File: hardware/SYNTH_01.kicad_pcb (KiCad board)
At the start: 2 copper layers, 112.7 x 150 mm, 100 parts, among them J2 Conn_01x04_Pin, SW1 SW_Push_45deg, SW10 SW_Push_45deg, SW11 SW_Push_45deg, SW12 SW_Push_45deg, SW13 SW_Push_45deg, SW14 SW_Push_45deg, SW15 SW_Push_45deg, SW16 SW_Push_45deg, SW17 SW_Push_45deg, SW18 SW_Push_45deg, SW19 SW_Push_45deg, SW2 SW_Push_45deg, SW20 SW_Push_45deg, SW21 SW_Push_45deg, SW3 SW_Push_45deg, SW4 SW_Push_45deg, SW5 SW_Push_45deg, SW6 SW_Push_45deg, SW7 SW_Push_45deg, SW8 SW_Push_45deg, SW9 SW_Push_45deg, U1 MCP23017-E/SP, U2 74AHCT1G125

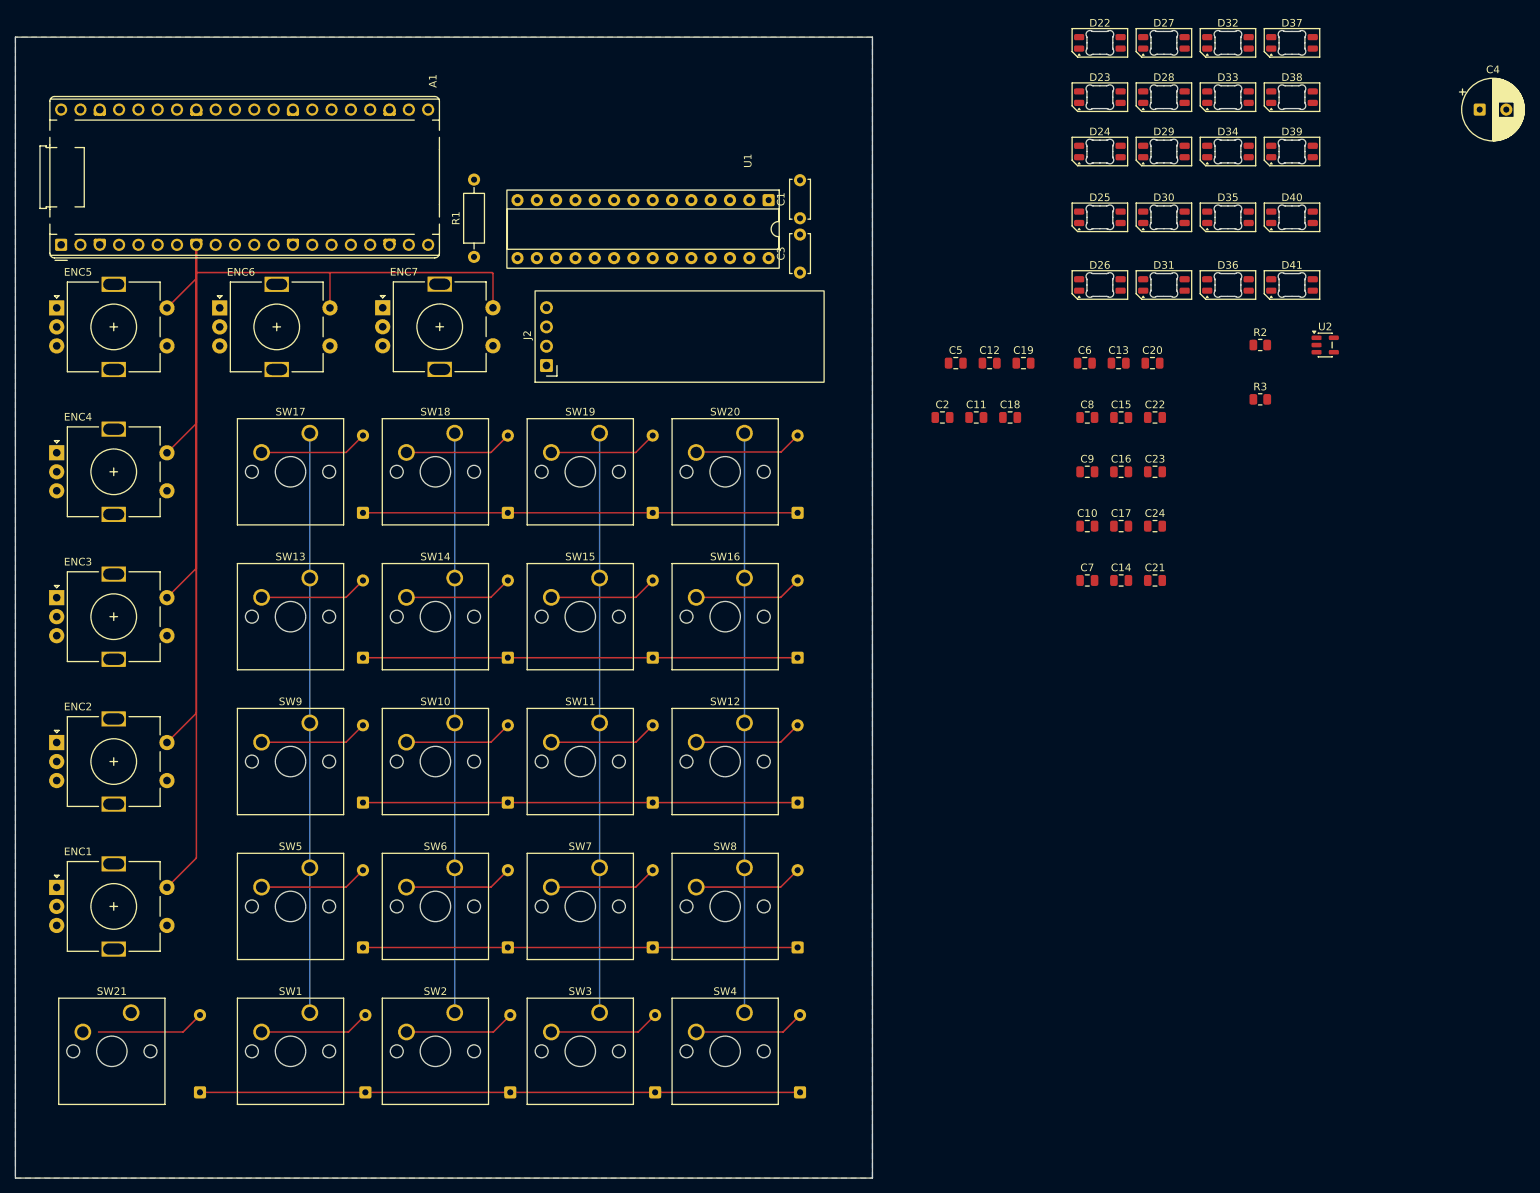
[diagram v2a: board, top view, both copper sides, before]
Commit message: PCB: connecting LEDs and their condensers in PCB view
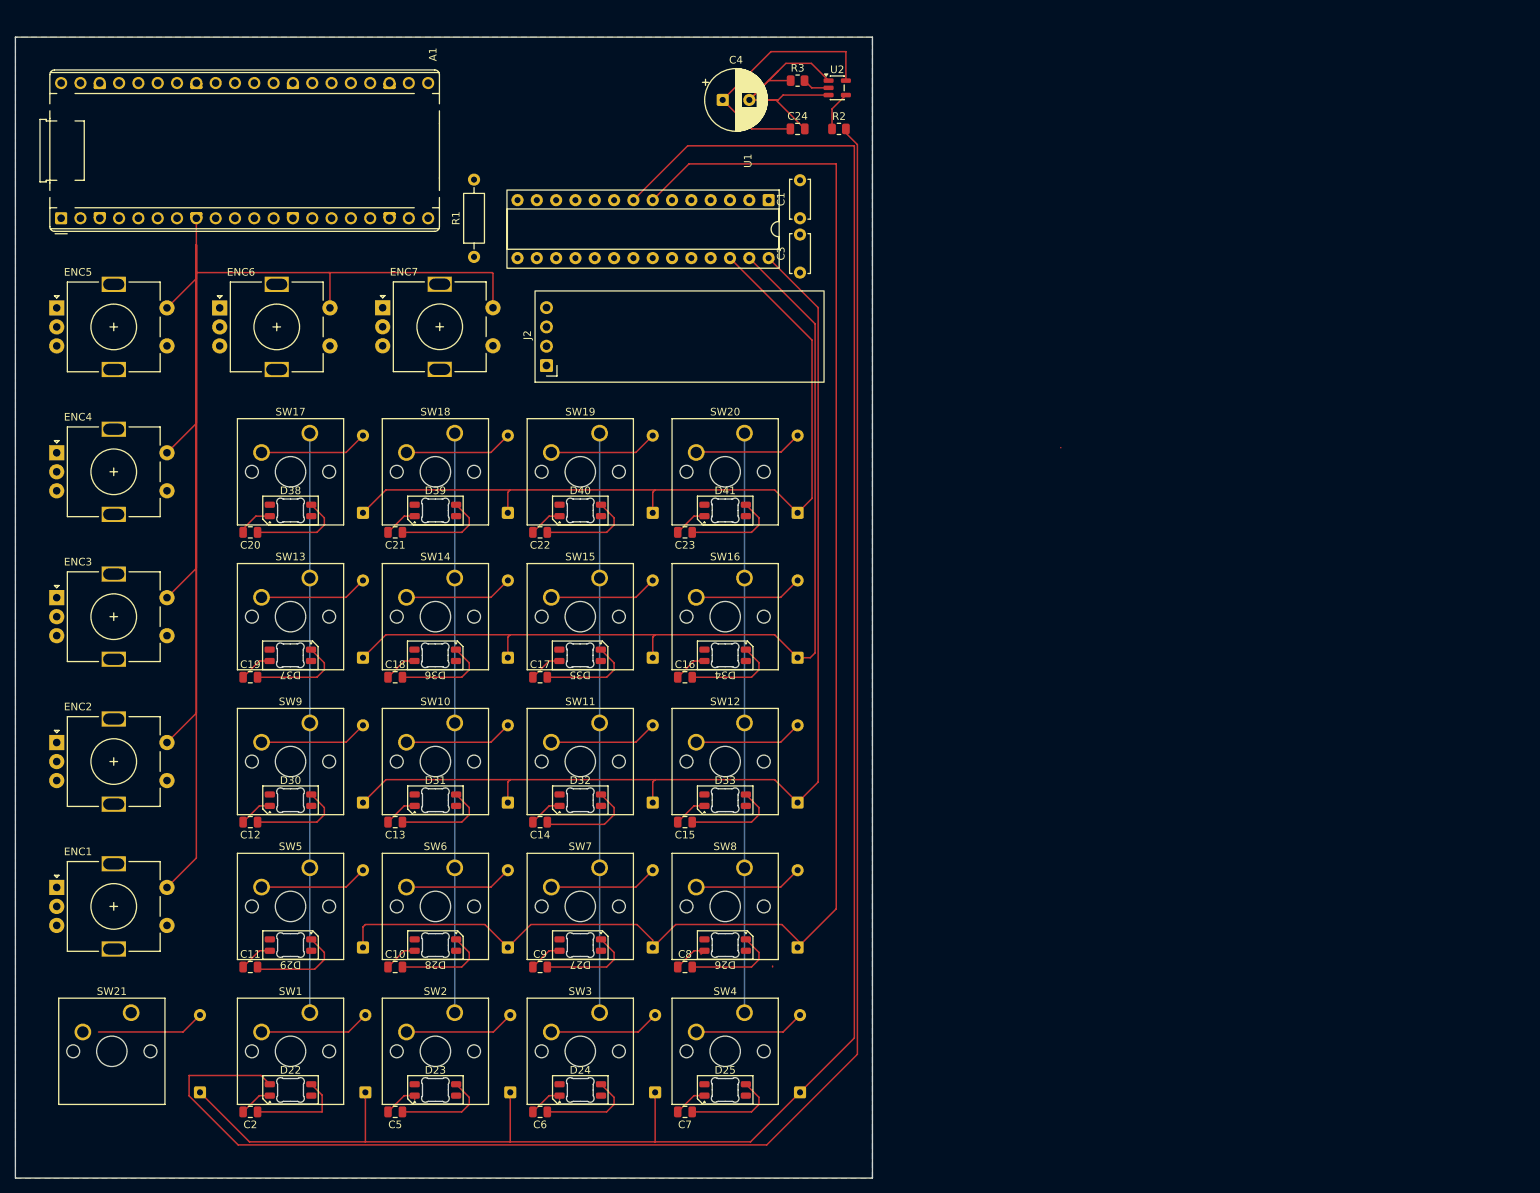
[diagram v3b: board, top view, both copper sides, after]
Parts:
- moved D22 174.0 mm to (80.6, 167.0)
- moved D23 157.1 mm to (99.7, 167.0)
- moved D29 155.2 mm to (80.6, 148.0), turned to 180 degrees
- moved D37 154.4 mm to (80.6, 109.9), turned to 180 degrees
- moved D28 147.0 mm to (99.7, 148.0), turned to 180 degrees
- moved D38 142.5 mm to (80.6, 90.8)
- moved D27 141.3 mm to (118.7, 148.0), turned to 180 degrees
- moved D24 141.0 mm to (118.7, 167.0)
- moved D30 138.1 mm to (80.6, 128.9)
- moved D32 131.0 mm to (118.7, 128.9)
- moved C2 128.9 mm to (75.4, 169.9), turned to 180 degrees
- moved D25 124.9 mm to (137.8, 167.0)
- moved C5 123.0 mm to (94.4, 169.9), turned to 180 degrees
- moved D39 122.1 mm to (99.7, 90.8)
- moved C6 121.7 mm to (113.5, 169.9), turned to 180 degrees
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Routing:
- net Net-(D22-DIN): track 0.00 -> 231.6 mm
- net LED_5V: track 0.00 -> 220.2 mm
- net GND: track 288.2 -> 488.1 mm
- net /SYNTH_01/ROW4: track 78.9 -> 263.2 mm
- net /SYNTH_01/ROW3: track 57.1 -> 198.8 mm
- net /SYNTH_01/ROW2: track 57.1 -> 141.4 mm
- net /SYNTH_01/ROW1: track 57.1 -> 124.0 mm
- net /SYNTH_01/ROW0: track 57.1 -> 104.7 mm
- net Net-(R2-Pad1): track 0.00 -> 5.21 mm
- net LED_DATA: track 0.00 -> 3.56 mm

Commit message: PCB: fixing visa duplicata
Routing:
- net /SYNTH_01/E2_SW: track 0.00 -> 195.7 mm, vias 0 -> 5
- net /SYNTH_01/E3_SW: track 0.00 -> 172.6 mm, vias 0 -> 2
- net /SYNTH_01/E4_SW: track 0.00 -> 143.6 mm, vias 0 -> 2
- net Net-(D25-DOUT): track 0.00 -> 72.5 mm, vias 0 -> 4
- net Net-(D23-DOUT): track 0.00 -> 15.6 mm, vias 0 -> 2
- net Net-(D24-DOUT): track 0.00 -> 15.2 mm, vias 0 -> 2
- net Net-(D22-DOUT): track 0.00 -> 15.2 mm, vias 0 -> 2
- net LED_5V: track 220.2 -> 225.6 mm

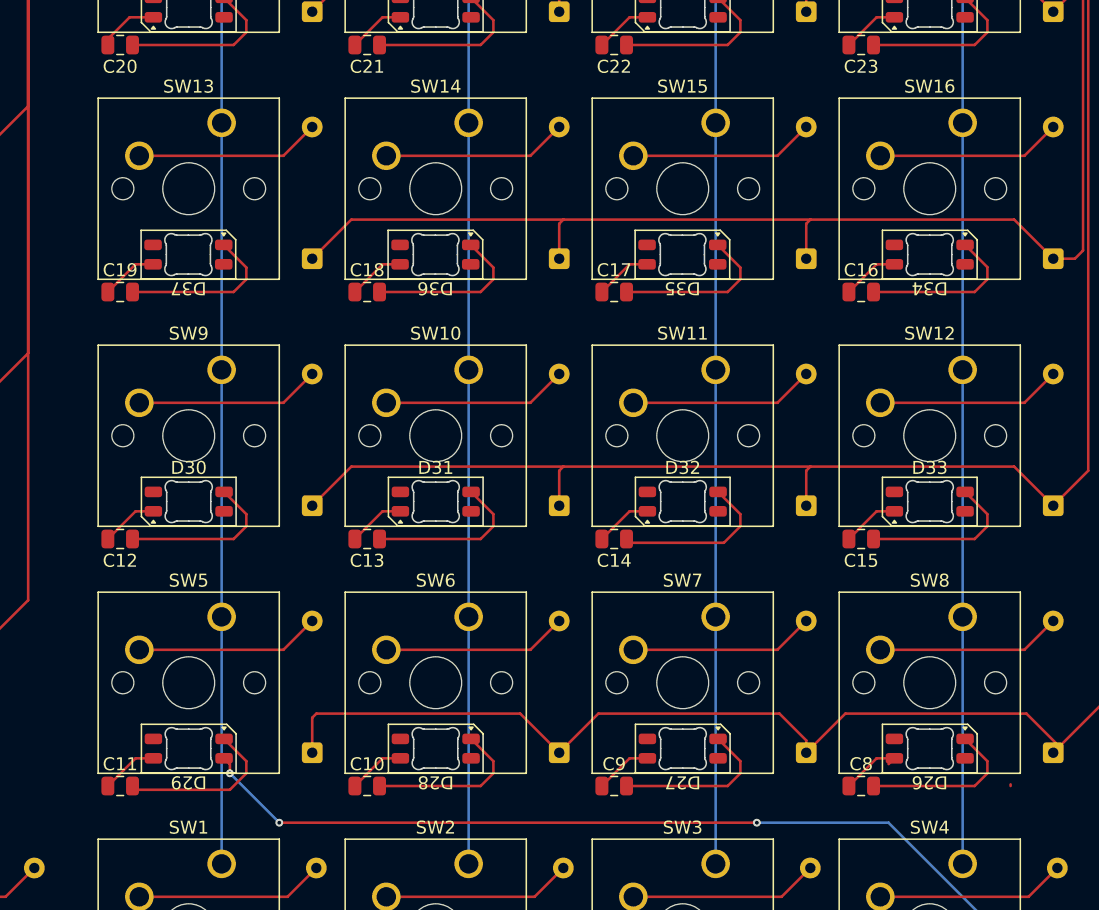
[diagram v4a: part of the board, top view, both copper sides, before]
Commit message: PCB: connection more LEDs
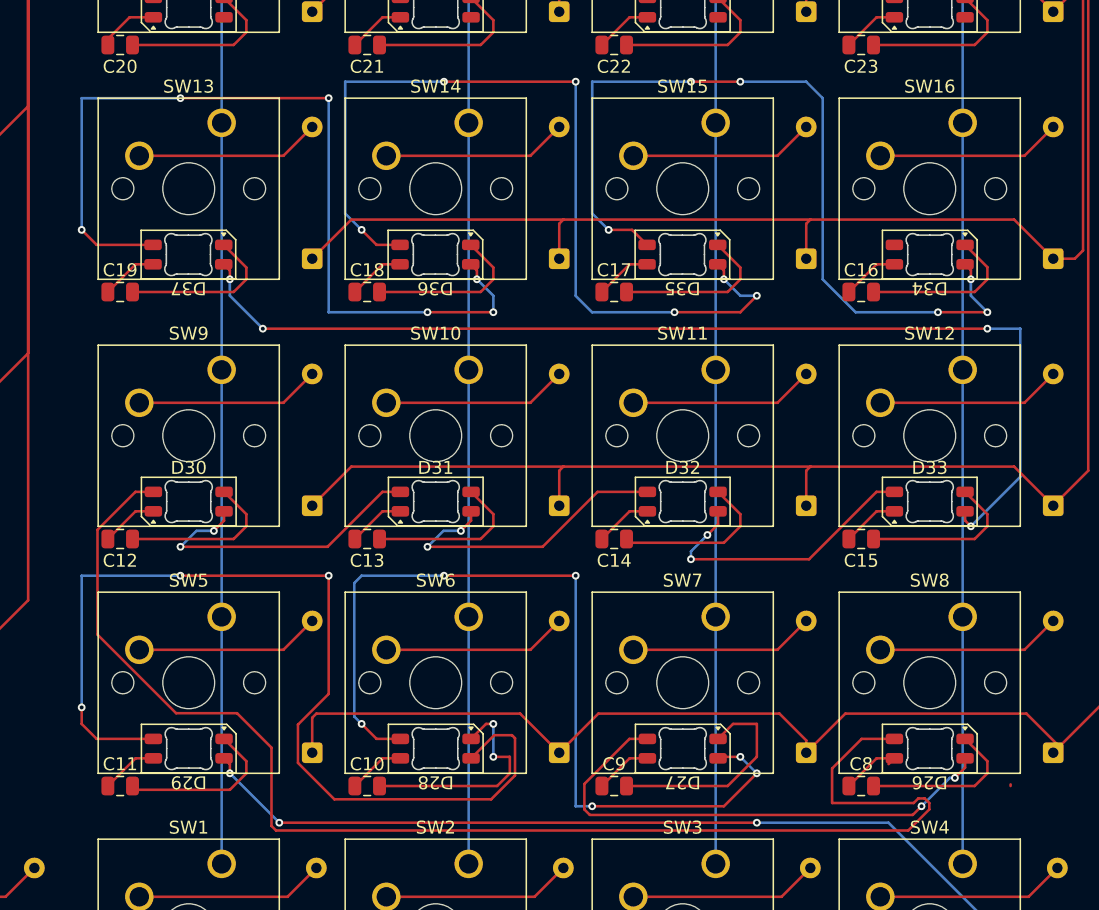
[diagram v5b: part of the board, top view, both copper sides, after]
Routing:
- net Net-(D26-DOUT): track 0.00 -> 104.9 mm
- net Net-(D33-DOUT): track 0.00 -> 82.8 mm, vias 0 -> 4
- net Net-(D28-DIN): track 0.00 -> 77.7 mm, vias 0 -> 3
- net Net-(D35-DIN): track 0.00 -> 69.1 mm, vias 0 -> 6
- net Net-(D36-DIN): track 0.00 -> 68.8 mm, vias 0 -> 6
- net Net-(D27-DIN): track 0.00 -> 68.6 mm, vias 0 -> 6
- net Net-(D34-DIN): track 0.00 -> 65.8 mm, vias 0 -> 6
- net Net-(D26-DIN): track 0.00 -> 40.0 mm, vias 0 -> 2
- net Net-(D31-DOUT): track 0.00 -> 23.6 mm, vias 0 -> 2
- net Net-(D30-DOUT): track 0.00 -> 23.6 mm, vias 0 -> 2
- net Net-(D32-DOUT): track 0.00 -> 22.4 mm, vias 0 -> 2
- net GND: track 488.1 -> 497.7 mm, vias 0 -> 2

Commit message: PCB: Checkpoint
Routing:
- net /SYNTH_01/E1_SW: track 0.00 -> 360.4 mm, vias 0 -> 2
- net GND: track 497.7 -> 668.3 mm, vias 2 -> 6
- net /SYNTH_01/COL_SHIFT: track 0.00 -> 168.7 mm
- net /SYNTH_01/E1_B: track 0.00 -> 112.7 mm, vias 0 -> 2
- net /SYNTH_01/E5_SW: track 0.00 -> 103.7 mm, vias 0 -> 2
- net /SYNTH_01/E1_A: track 0.00 -> 100.6 mm
- net /SYNTH_01/E2_B: track 0.00 -> 98.8 mm, vias 0 -> 2
- net Net-(D34-DOUT): track 0.00 -> 91.5 mm
- net /SYNTH_01/E2_A: track 0.00 -> 86.4 mm, vias 0 -> 2
- net /SYNTH_01/E6_SW: track 0.00 -> 80.8 mm, vias 0 -> 1
- net /SYNTH_01/COL1: track 76.2 -> 150.9 mm, vias 0 -> 2
- net /SYNTH_01/E3_B: track 0.00 -> 73.2 mm, vias 0 -> 1
- net /SYNTH_01/E3_A: track 0.00 -> 72.4 mm
- net /SYNTH_01/E5_B: track 0.00 -> 62.0 mm, vias 0 -> 2
- net /SYNTH_01/COL0: track 76.2 -> 132.5 mm, vias 0 -> 2
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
